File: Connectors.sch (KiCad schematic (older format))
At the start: 4 parts

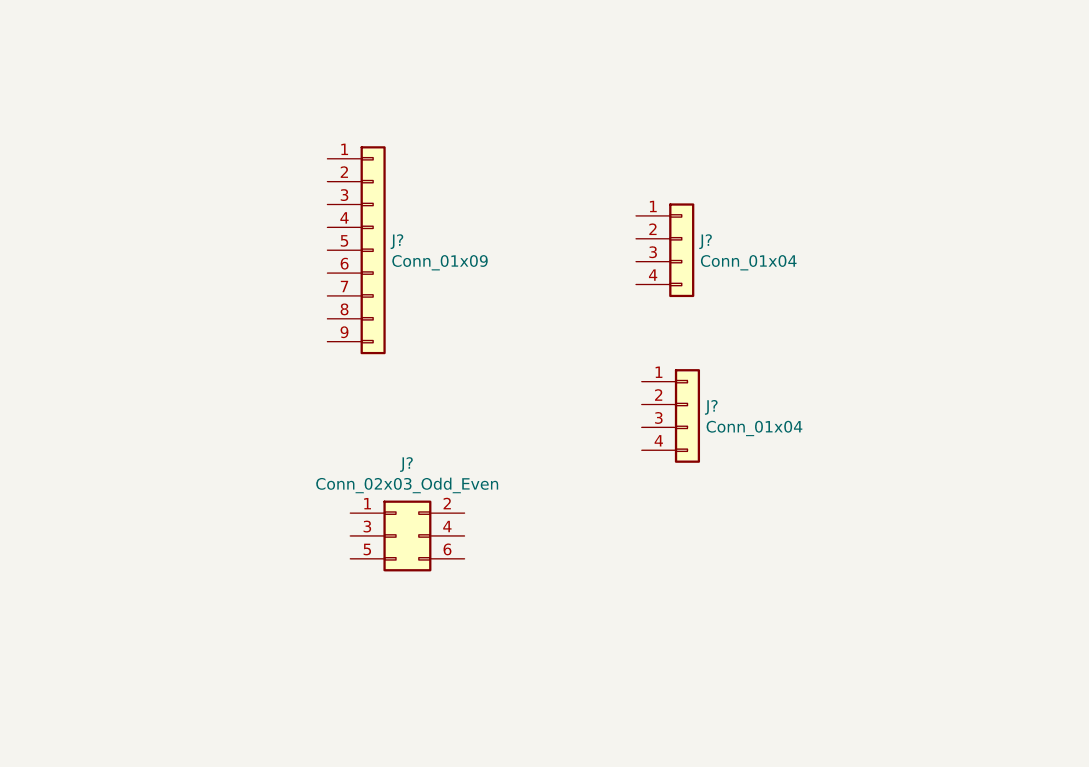
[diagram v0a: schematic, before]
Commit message: Arranged symbols.
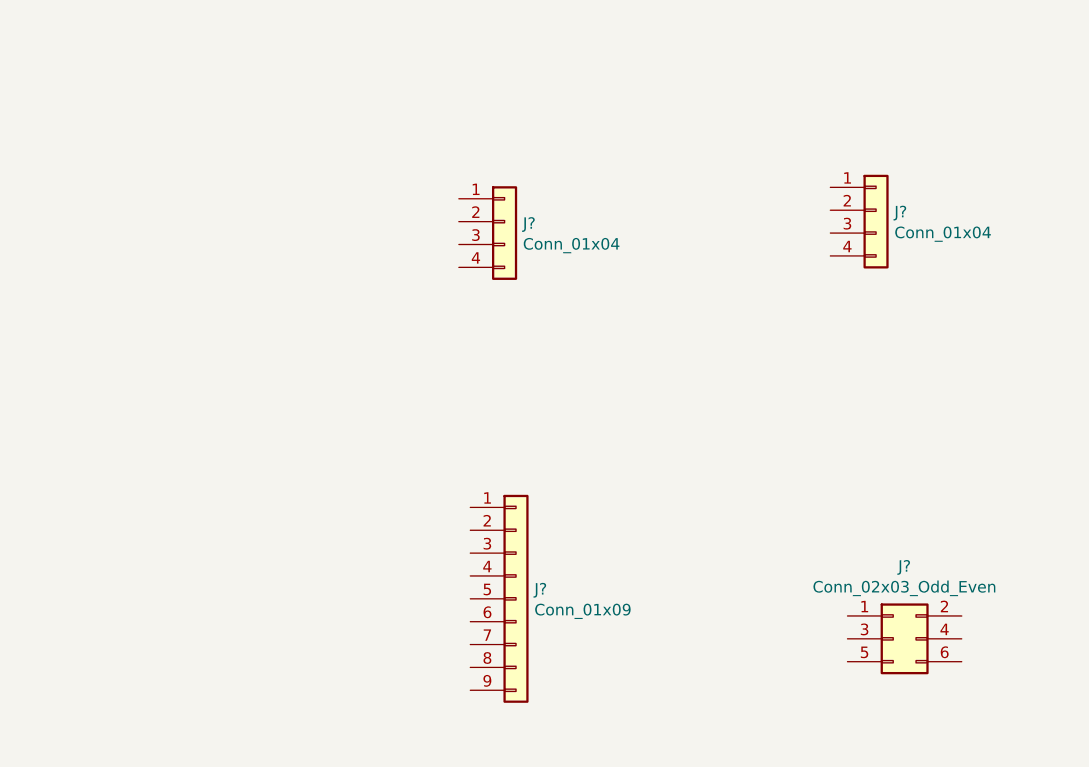
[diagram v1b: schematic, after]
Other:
- moved on the sheet: J?
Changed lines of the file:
@@
 L Connector_Generic:Conn_01x09 J?
 U 1 1 60D7775B
-P 4375 2925
-F 0 "J?" H 4455 2967 50  0000 L CNN
-F 1 "Conn_01x09" H 4455 2876 50  0000 L CNN
-F 2 "" H 4375 2925 50  0001 C CNN
-F 3 "~" H 4375 2925 50  0001 C CNN
-	1    4375 2925
+P 5000 4450
+F 0 "J?" H 5080 4492 50  0000 L CNN
+F 1 "Conn_01x09" H 5080 4401 50  0000 L CNN
+F 2 "" H 5000 4450 50  0001 C CNN
+F 3 "~" H 5000 4450 50  0001 C CNN
+	1    5000 4450
 	1    0    0    -1
 $EndComp
@@
 L Connector_Generic:Conn_01x04 J?
 U 1 1 60D7857C
-P 5725 2875
-F 0 "J?" H 5805 2867 50  0000 L CNN
-F 1 "Conn_01x04" H 5805 2776 50  0000 L CNN
-F 2 "" H 5725 2875 50  0001 C CNN
-F 3 "~" H 5725 2875 50  0001 C CNN
-	1    5725 2875
+P 4950 2800
+F 0 "J?" H 5030 2792 50  0000 L CNN
+F 1 "Conn_01x04" H 5030 2701 50  0000 L CNN
+F 2 "" H 4950 2800 50  0001 C CNN
+F 3 "~" H 4950 2800 50  0001 C CNN
+	1    4950 2800
 	1    0    0    -1
 $EndComp
@@
 L Connector_Generic:Conn_01x04 J?
 U 1 1 60D78A32
-P 5750 3600
-F 0 "J?" H 5830 3592 50  0000 L CNN
-F 1 "Conn_01x04" H 5830 3501 50  0000 L CNN
-F 2 "" H 5750 3600 50  0001 C CNN
-F 3 "~" H 5750 3600 50  0001 C CNN
-	1    5750 3600
+P 6575 2750
+F 0 "J?" H 6655 2742 50  0000 L CNN
+F 1 "Conn_01x04" H 6655 2651 50  0000 L CNN
+F 2 "" H 6575 2750 50  0001 C CNN
+F 3 "~" H 6575 2750 50  0001 C CNN
+	1    6575 2750
 	1    0    0    -1
 $EndComp
@@
 L Connector_Generic:Conn_02x03_Odd_Even J?
 U 1 1 60D796C8
-P 4475 4175
-F 0 "J?" H 4525 4492 50  0000 C CNN
-F 1 "Conn_02x03_Odd_Even" H 4525 4401 50  0000 C CNN
-F 2 "" H 4475 4175 50  0001 C CNN
-F 3 "~" H 4475 4175 50  0001 C CNN
-	1    4475 4175
+P 6650 4625
+F 0 "J?" H 6700 4942 50  0000 C CNN
+F 1 "Conn_02x03_Odd_Even" H 6700 4851 50  0000 C CNN
+F 2 "" H 6650 4625 50  0001 C CNN
+F 3 "~" H 6650 4625 50  0001 C CNN
+	1    6650 4625
 	1    0    0    -1
 $EndComp

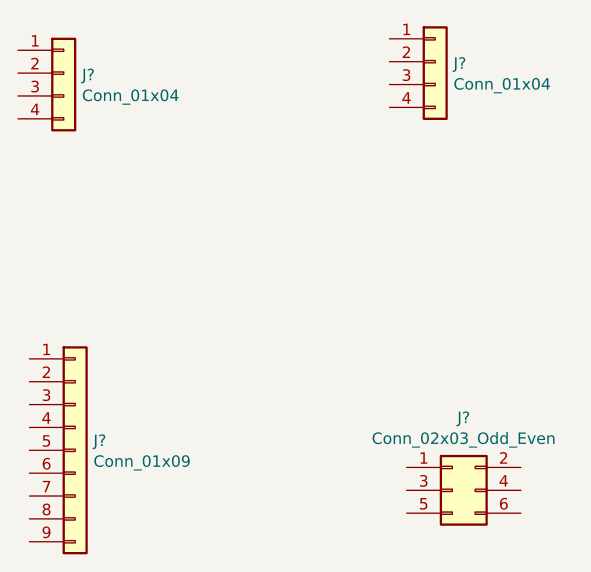
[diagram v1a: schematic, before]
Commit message: Annotated symbols.
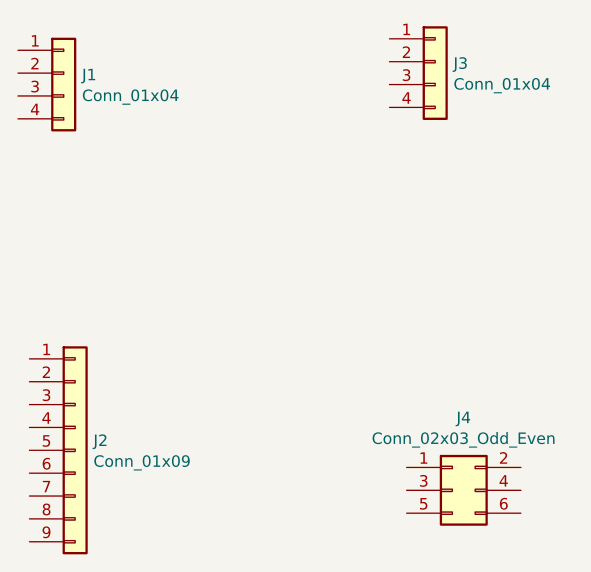
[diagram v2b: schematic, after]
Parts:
- gave numbers to parts that had none: 4
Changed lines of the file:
@@
 $EndDescr
 $Comp
-L Connector_Generic:Conn_01x09 J?
+L Connector_Generic:Conn_01x09 J2
 U 1 1 60D7775B
 P 5000 4450
-F 0 "J?" H 5080 4492 50  0000 L CNN
+F 0 "J2" H 5080 4492 50  0000 L CNN
 F 1 "Conn_01x09" H 5080 4401 50  0000 L CNN
 F 2 "" H 5000 4450 50  0001 C CNN
@@
 $EndComp
 $Comp
-L Connector_Generic:Conn_01x04 J?
+L Connector_Generic:Conn_01x04 J1
 U 1 1 60D7857C
 P 4950 2800
-F 0 "J?" H 5030 2792 50  0000 L CNN
+F 0 "J1" H 5030 2792 50  0000 L CNN
 F 1 "Conn_01x04" H 5030 2701 50  0000 L CNN
 F 2 "" H 4950 2800 50  0001 C CNN
@@
 $EndComp
 $Comp
-L Connector_Generic:Conn_01x04 J?
+L Connector_Generic:Conn_01x04 J3
 U 1 1 60D78A32
 P 6575 2750
-F 0 "J?" H 6655 2742 50  0000 L CNN
+F 0 "J3" H 6655 2742 50  0000 L CNN
 F 1 "Conn_01x04" H 6655 2651 50  0000 L CNN
 F 2 "" H 6575 2750 50  0001 C CNN
@@
 $EndComp
 $Comp
-L Connector_Generic:Conn_02x03_Odd_Even J?
+L Connector_Generic:Conn_02x03_Odd_Even J4
 U 1 1 60D796C8
 P 6650 4625
-F 0 "J?" H 6700 4942 50  0000 C CNN
+F 0 "J4" H 6700 4942 50  0000 C CNN
 F 1 "Conn_02x03_Odd_Even" H 6700 4851 50  0000 C CNN
 F 2 "" H 6650 4625 50  0001 C CNN

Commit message: Completed footprint associations and added component values.
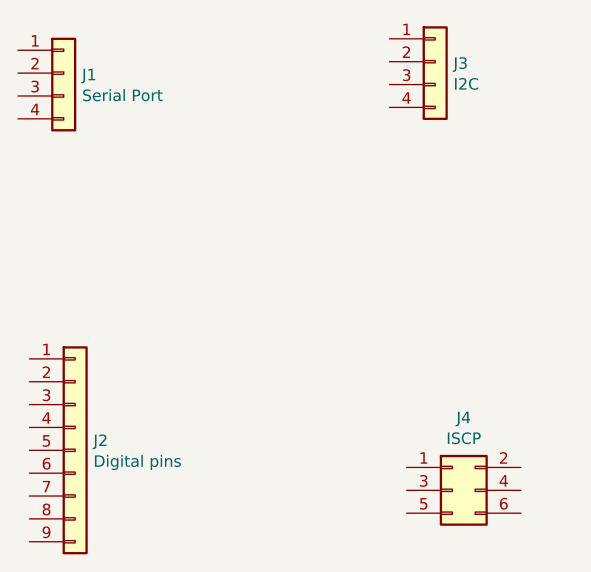
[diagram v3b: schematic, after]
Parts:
- J1: value Conn_01x04 -> Serial Port; footprint (none) -> Connector_PinHeader_2.54mm:PinHeader_1x04_P2.54mm_Vertical
- J2: value Conn_01x09 -> Digital pins; footprint (none) -> Connector_PinHeader_2.54mm:PinHeader_1x09_P2.54mm_Vertical
- J3: value Conn_01x04 -> I2C; footprint (none) -> Connector_PinHeader_2.54mm:PinHeader_1x04_P2.54mm_Vertical
- J4: value Conn_02x03_Odd_Even -> ISCP; footprint (none) -> Connector_PinHeader_2.54mm:PinHeader_2x03_P2.54mm_Vertical
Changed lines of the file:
@@
 P 5000 4450
 F 0 "J2" H 5080 4492 50  0000 L CNN
-F 1 "Conn_01x09" H 5080 4401 50  0000 L CNN
-F 2 "" H 5000 4450 50  0001 C CNN
+F 1 "Digital pins" H 5080 4401 50  0000 L CNN
+F 2 "Connector_PinHeader_2.54mm:PinHeader_1x09_P2.54mm_Vertical" H 5000 4450 50  0001 C CNN
 F 3 "~" H 5000 4450 50  0001 C CNN
 	1    5000 4450
@@
 P 4950 2800
 F 0 "J1" H 5030 2792 50  0000 L CNN
-F 1 "Conn_01x04" H 5030 2701 50  0000 L CNN
-F 2 "" H 4950 2800 50  0001 C CNN
+F 1 "Serial Port" H 5030 2701 50  0000 L CNN
+F 2 "Connector_PinHeader_2.54mm:PinHeader_1x04_P2.54mm_Vertical" H 4950 2800 50  0001 C CNN
 F 3 "~" H 4950 2800 50  0001 C CNN
 	1    4950 2800
@@
 P 6575 2750
 F 0 "J3" H 6655 2742 50  0000 L CNN
-F 1 "Conn_01x04" H 6655 2651 50  0000 L CNN
-F 2 "" H 6575 2750 50  0001 C CNN
+F 1 "I2C" H 6655 2651 50  0000 L CNN
+F 2 "Connector_PinHeader_2.54mm:PinHeader_1x04_P2.54mm_Vertical" H 6575 2750 50  0001 C CNN
 F 3 "~" H 6575 2750 50  0001 C CNN
 	1    6575 2750
@@
 P 6650 4625
 F 0 "J4" H 6700 4942 50  0000 C CNN
-F 1 "Conn_02x03_Odd_Even" H 6700 4851 50  0000 C CNN
-F 2 "" H 6650 4625 50  0001 C CNN
+F 1 "ISCP" H 6700 4851 50  0000 C CNN
+F 2 "Connector_PinHeader_2.54mm:PinHeader_2x03_P2.54mm_Vertical" H 6650 4625 50  0001 C CNN
 F 3 "~" H 6650 4625 50  0001 C CNN
 	1    6650 4625

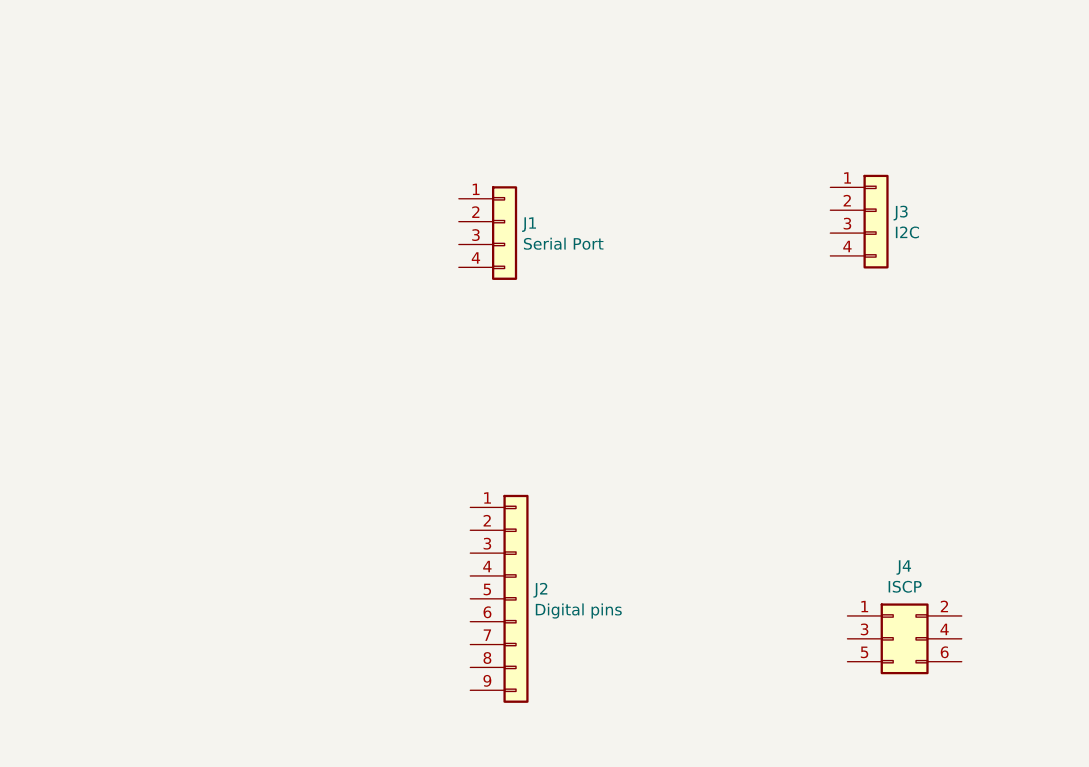
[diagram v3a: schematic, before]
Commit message: Completed wiring in connector sheet.
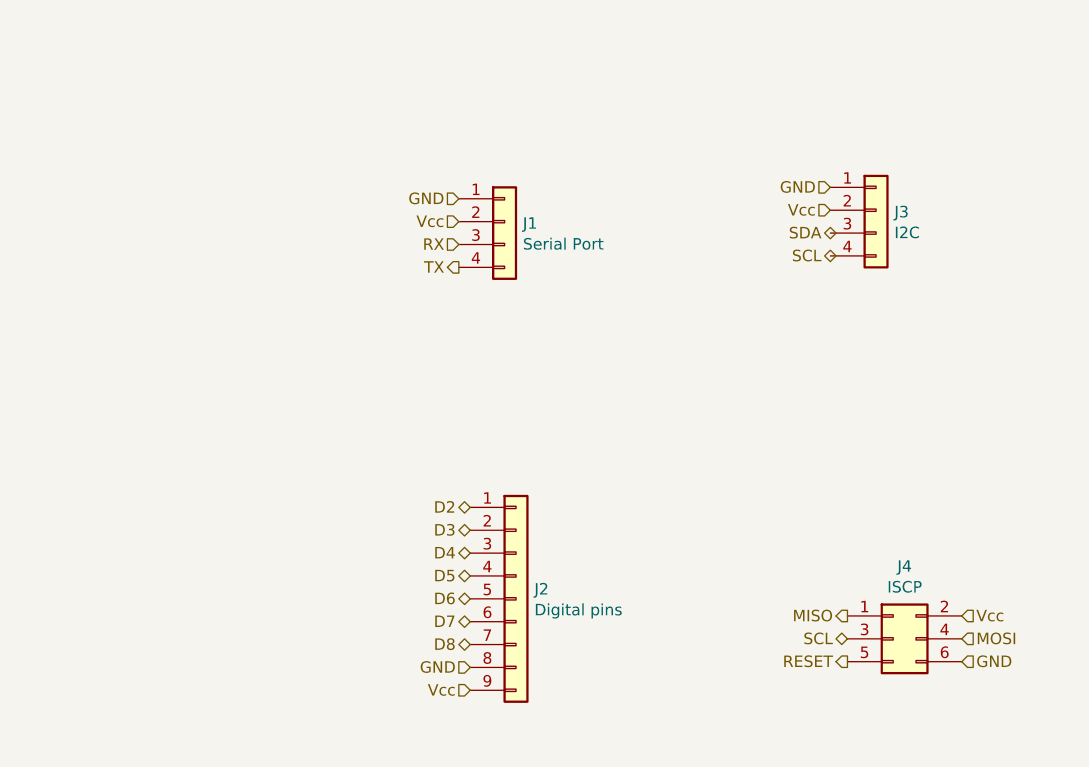
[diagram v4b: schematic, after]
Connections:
- net D2: now reaches J2.1 (Pin_1)
- net D3: now reaches J2.2 (Pin_2)
- net D4: now reaches J2.3 (Pin_3)
- net D5: now reaches J2.4 (Pin_4)
- net D6: now reaches J2.5 (Pin_5)
- net D7: now reaches J2.6 (Pin_6)
- net D8: now reaches J2.7 (Pin_7)
- net GND: now reaches J2.8 (Pin_8)
- net GND: now also J1.1 (Pin_1), J3.1 (Pin_1), J4.6 (Pin_6)
- net Vcc: now reaches J2.9 (Pin_9)
- net Vcc: now also J1.2 (Pin_2), J3.2 (Pin_2), J4.2 (Pin_2)
- net RX: now reaches J1.3 (Pin_3)
- net TX: now reaches J1.4 (Pin_4)
- net MISO: now reaches J4.1 (Pin_1)
- net SCL: now reaches J4.3 (Pin_3)
- net MOSI: now reaches J4.4 (Pin_4)
- net RESET: now reaches J4.5 (Pin_5)
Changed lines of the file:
@@
 encoding utf-8
 Sheet 2 2
-Title "Battery Powered Aduino Clone with Clock & Extended EEPROM"
+Title "Battery Powered Arduino Clone with Clock & Extended EEPROM"
 Date "2021-06-24"
 Rev "1"
@@
 	1    0    0    -1
 $EndComp
+Text HLabel 6450 4525 0    50   Output ~ 0
+MISO
+Text HLabel 6450 4625 0    50   BiDi ~ 0
+SCL
+Text HLabel 6450 4725 0    50   Output ~ 0
+RESET
+Text HLabel 6950 4525 2    50   Input ~ 0
+Vcc
+Text HLabel 6950 4625 2    50   Input ~ 0
+MOSI
+Text HLabel 6950 4725 2    50   Input ~ 0
+GND
+Text HLabel 4750 2700 0    50   Input ~ 0
+GND
+Text HLabel 4750 2800 0    50   Input ~ 0
+Vcc
+Text HLabel 4750 2900 0    50   Input ~ 0
+RX
+Text HLabel 4750 3000 0    50   Output ~ 0
+TX
+Text HLabel 6375 2650 0    50   Input ~ 0
+GND
+Text HLabel 6375 2750 0    50   Input ~ 0
+Vcc
+Text HLabel 6400 2850 0    50   BiDi ~ 0
+SDA
+Text HLabel 6400 2950 0    50   BiDi ~ 0
+SCL
+Text HLabel 4800 4050 0    50   BiDi ~ 0
+D2
+Text HLabel 4800 4150 0    50   BiDi ~ 0
+D3
+Text HLabel 4800 4250 0    50   BiDi ~ 0
+D4
+Text HLabel 4800 4350 0    50   BiDi ~ 0
+D5
+Text HLabel 4800 4450 0    50   BiDi ~ 0
+D6
+Text HLabel 4800 4550 0    50   BiDi ~ 0
+D7
+Text HLabel 4800 4650 0    50   BiDi ~ 0
+D8
+Text HLabel 4800 4750 0    50   Input ~ 0
+GND
+Text HLabel 4800 4850 0    50   Input ~ 0
+Vcc
 $EndSCHEMATC

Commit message: Completed wiring in root sheet. Fixed DRC all errors.
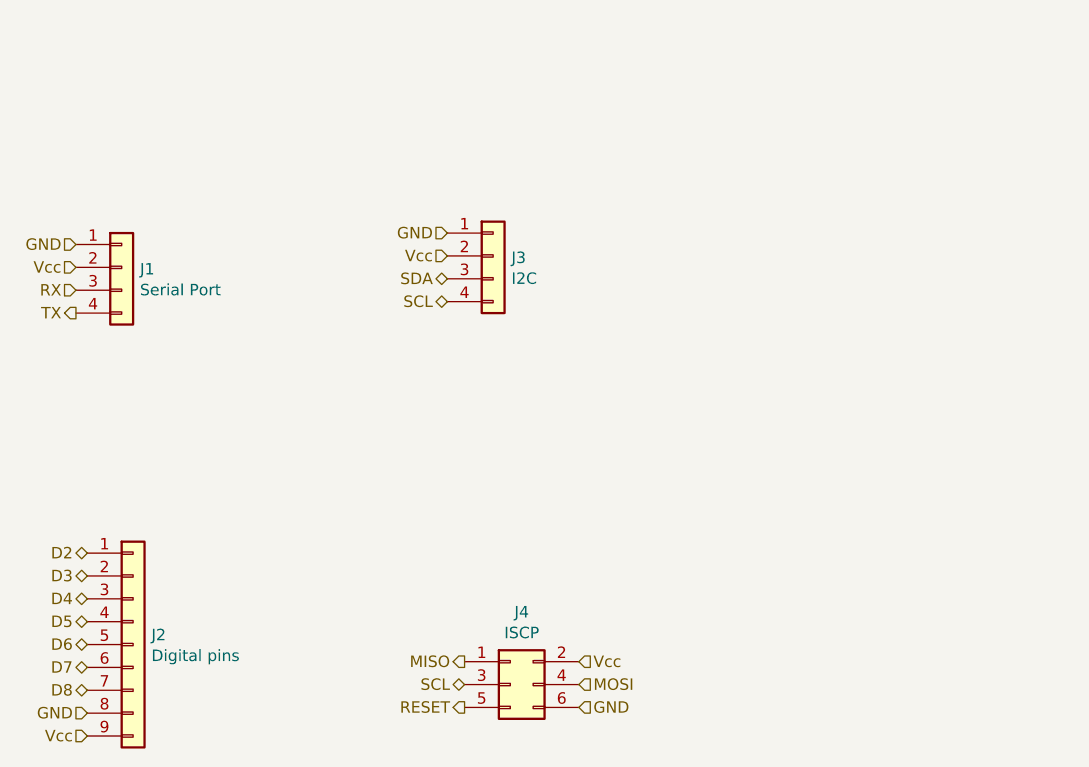
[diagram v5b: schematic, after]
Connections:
- net SCL: now also J3.4 (Pin_4)
- net SDA: now also J3.3 (Pin_3)
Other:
- moved on the sheet: J1, J2, J3, J4
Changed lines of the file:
@@
 L Connector_Generic:Conn_01x09 J2
 U 1 1 60D7775B
-P 5000 4450
-F 0 "J2" H 5080 4492 50  0000 L CNN
-F 1 "Digital pins" H 5080 4401 50  0000 L CNN
-F 2 "Connector_PinHeader_2.54mm:PinHeader_1x09_P2.54mm_Vertical" H 5000 4450 50  0001 C CNN
-F 3 "~" H 5000 4450 50  0001 C CNN
-	1    5000 4450
+P 3325 4650
+F 0 "J2" H 3405 4692 50  0000 L CNN
+F 1 "Digital pins" H 3405 4601 50  0000 L CNN
+F 2 "Connector_PinHeader_2.54mm:PinHeader_1x09_P2.54mm_Vertical" H 3325 4650 50  0001 C CNN
+F 3 "~" H 3325 4650 50  0001 C CNN
+	1    3325 4650
 	1    0    0    -1
 $EndComp
@@
 L Connector_Generic:Conn_01x04 J1
 U 1 1 60D7857C
-P 4950 2800
-F 0 "J1" H 5030 2792 50  0000 L CNN
-F 1 "Serial Port" H 5030 2701 50  0000 L CNN
-F 2 "Connector_PinHeader_2.54mm:PinHeader_1x04_P2.54mm_Vertical" H 4950 2800 50  0001 C CNN
-F 3 "~" H 4950 2800 50  0001 C CNN
-	1    4950 2800
+P 3275 3000
+F 0 "J1" H 3355 2992 50  0000 L CNN
+F 1 "Serial Port" H 3355 2901 50  0000 L CNN
+F 2 "Connector_PinHeader_2.54mm:PinHeader_1x04_P2.54mm_Vertical" H 3275 3000 50  0001 C CNN
+F 3 "~" H 3275 3000 50  0001 C CNN
+	1    3275 3000
 	1    0    0    -1
 $EndComp
@@
 L Connector_Generic:Conn_01x04 J3
 U 1 1 60D78A32
-P 6575 2750
-F 0 "J3" H 6655 2742 50  0000 L CNN
-F 1 "I2C" H 6655 2651 50  0000 L CNN
-F 2 "Connector_PinHeader_2.54mm:PinHeader_1x04_P2.54mm_Vertical" H 6575 2750 50  0001 C CNN
-F 3 "~" H 6575 2750 50  0001 C CNN
-	1    6575 2750
+P 4900 2950
+F 0 "J3" H 4980 2942 50  0000 L CNN
+F 1 "I2C" H 4980 2851 50  0000 L CNN
+F 2 "Connector_PinHeader_2.54mm:PinHeader_1x04_P2.54mm_Vertical" H 4900 2950 50  0001 C CNN
+F 3 "~" H 4900 2950 50  0001 C CNN
+	1    4900 2950
 	1    0    0    -1
 $EndComp
@@
 L Connector_Generic:Conn_02x03_Odd_Even J4
 U 1 1 60D796C8
-P 6650 4625
-F 0 "J4" H 6700 4942 50  0000 C CNN
-F 1 "ISCP" H 6700 4851 50  0000 C CNN
-F 2 "Connector_PinHeader_2.54mm:PinHeader_2x03_P2.54mm_Vertical" H 6650 4625 50  0001 C CNN
-F 3 "~" H 6650 4625 50  0001 C CNN
-	1    6650 4625
+P 4975 4825
+F 0 "J4" H 5025 5142 50  0000 C CNN
+F 1 "ISCP" H 5025 5051 50  0000 C CNN
+F 2 "Connector_PinHeader_2.54mm:PinHeader_2x03_P2.54mm_Vertical" H 4975 4825 50  0001 C CNN
+F 3 "~" H 4975 4825 50  0001 C CNN
+	1    4975 4825
 	1    0    0    -1
 $EndComp
-Text HLabel 6450 4525 0    50   Output ~ 0
+Text HLabel 4775 4725 0    50   Output ~ 0
 MISO
-Text HLabel 6450 4625 0    50   BiDi ~ 0
+Text HLabel 4775 4825 0    50   BiDi ~ 0
 SCL
-Text HLabel 6450 4725 0    50   Output ~ 0
+Text HLabel 4775 4925 0    50   Output ~ 0
 RESET
-Text HLabel 6950 4525 2    50   Input ~ 0
+Text HLabel 5275 4725 2    50   Input ~ 0
 Vcc
-Text HLabel 6950 4625 2    50   Input ~ 0
+Text HLabel 5275 4825 2    50   Input ~ 0
 MOSI
-Text HLabel 6950 4725 2    50   Input ~ 0
+Text HLabel 5275 4925 2    50   Input ~ 0
 GND
-Text HLabel 4750 2700 0    50   Input ~ 0
+Text HLabel 3075 2900 0    50   Input ~ 0
 GND
-Text HLabel 4750 2800 0    50   Input ~ 0
+Text HLabel 3075 3000 0    50   Input ~ 0
 Vcc
-Text HLabel 4750 2900 0    50   Input ~ 0
+Text HLabel 3075 3100 0    50   Input ~ 0
 RX
-Text HLabel 4750 3000 0    50   Output ~ 0
+Text HLabel 3075 3200 0    50   Output ~ 0
 TX
-Text HLabel 6375 2650 0    50   Input ~ 0
+Text HLabel 4700 2850 0    50   Input ~ 0
 GND
-Text HLabel 6375 2750 0    50   Input ~ 0
+Text HLabel 4700 2950 0    50   Input ~ 0
 Vcc
-Text HLabel 6400 2850 0    50   BiDi ~ 0
+Text HLabel 4700 3050 0    50   BiDi ~ 0
 SDA
-Text HLabel 6400 2950 0    50   BiDi ~ 0
+Text HLabel 4700 3150 0    50   BiDi ~ 0
 SCL
-Text HLabel 4800 4050 0    50   BiDi ~ 0
+Text HLabel 3125 4250 0    50   BiDi ~ 0
 D2
-Text HLabel 4800 4150 0    50   BiDi ~ 0
+Text HLabel 3125 4350 0    50   BiDi ~ 0
 D3
-Text HLabel 4800 4250 0    50   BiDi ~ 0
+Text HLabel 3125 4450 0    50   BiDi ~ 0
 D4
-Text HLabel 4800 4350 0    50   BiDi ~ 0
+Text HLabel 3125 4550 0    50   BiDi ~ 0
 D5
-Text HLabel 4800 4450 0    50   BiDi ~ 0
+Text HLabel 3125 4650 0    50   BiDi ~ 0
 D6
-Text HLabel 4800 4550 0    50   BiDi ~ 0
+Text HLabel 3125 4750 0    50   BiDi ~ 0
 D7
-Text HLabel 4800 4650 0    50   BiDi ~ 0
+Text HLabel 3125 4850 0    50   BiDi ~ 0
 D8
-Text HLabel 4800 4750 0    50   Input ~ 0
+Text HLabel 3125 4950 0    50   Input ~ 0
 GND
-Text HLabel 4800 4850 0    50   Input ~ 0
+Text HLabel 3125 5050 0    50   Input ~ 0
 Vcc
 $EndSCHEMATC
